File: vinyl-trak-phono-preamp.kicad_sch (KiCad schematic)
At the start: 79 parts, among them J1 Conn_01x03_Pin, J2 Screw_Terminal_01x03, J3 Screw_Terminal_01x02, J4 Screw_Terminal_01x02, Q1 2N3906, Q10 2N3906, Q11 JFE2140D, Q12 2N5089, Q13 2N3904, Q14 2N3904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

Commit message: Revision 0.1
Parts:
- removed C1: 0.015u, symbol Device:C
- removed C2: 100p, Capacitor_SMD:C_0805_2012Metric_Pad1.18x1.45mm_HandSolder, symbol Device:C
- removed C3: 0.005u, symbol Device:C
- removed C4: 0.015u, Capacitor_SMD:C_0805_2012Metric_Pad1.18x1.45mm_HandSolder, symbol Device:C
- removed C6: 1u, Capacitor_SMD:C_0805_2012Metric_Pad1.18x1.45mm_HandSolder, symbol Device:C
- removed C7, C8: 10n, Capacitor_SMD:C_0805_2012Metric_Pad1.18x1.45mm_HandSolder, symbol Device:C
- removed C9: 0.020u, Capacitor_SMD:C_0805_2012Metric_Pad1.18x1.45mm_HandSolder, symbol Device:C
- removed D1, D2: D, Diode_SMD:D_0805_2012Metric_Pad1.15x1.40mm_HandSolder, symbol Device:D
- removed J1: Conn_01x03_Pin, Connector_PinHeader_1.27mm:PinHeader_1x03_P1.27mm_Vertical, symbol Connector:Conn_01x03_Pin
- removed J2: Screw_Terminal_01x03, TerminalBlock_4Ucon:TerminalBlock_4Ucon_1x03_P3.50mm_Horizontal, symbol Connector:Screw_Terminal_01x03
- removed J3: Screw_Terminal_01x02, TerminalBlock_4Ucon:TerminalBlock_4Ucon_1x02_P3.50mm_Horizontal, symbol Connector:Screw_Terminal_01x02
- removed Q1, Q10, Q3, Q4, Q8: 2N3906, Library:SOT-23_Handsoldering-adjusted-pinout, symbol Simulation_SPICE:PNP
- removed Q11: JFE2140D, Package_SO:SOIC-8_3.9x4.9mm_P1.27mm, symbol Transistor_FET:JFE2140D
- removed Q12, Q15, Q18, Q19, Q21: 2N5089, Library:SOT-23_Handsoldering-adjusted-pinout, symbol Simulation_SPICE:NPN
- removed Q13, Q14, Q2, Q5, Q6, Q7, Q9: 2N3904, Library:SOT-23_Handsoldering-adjusted-pinout, symbol Simulation_SPICE:NPN
- removed Q16, Q17, Q20: 2N5087, Library:SOT-23_Handsoldering-adjusted-pinout, symbol Simulation_SPICE:PNP
- removed R1, R3: 100k, Resistor_SMD:R_0805_2012Metric_Pad1.20x1.40mm_HandSolder, symbol Device:R
- removed R10, R11: 600, Resistor_SMD:R_0805_2012Metric_Pad1.20x1.40mm_HandSolder, symbol Device:R
- removed R12, R13, R17, R8, R9: 220, Resistor_SMD:R_0805_2012Metric_Pad1.20x1.40mm_HandSolder, symbol Device:R
- removed R14, R19, R23, R24: 1k47, Resistor_SMD:R_0805_2012Metric_Pad1.20x1.40mm_HandSolder, symbol Device:R
- removed R15, R20: 100, Resistor_SMD:R_0805_2012Metric_Pad1.20x1.40mm_HandSolder, symbol Device:R
- removed R16: 71k5, Resistor_SMD:R_0805_2012Metric_Pad1.20x1.40mm_HandSolder, symbol Device:R
- removed R18: 160, Resistor_SMD:R_0805_2012Metric_Pad1.20x1.40mm_HandSolder, symbol Device:R
- removed R2: 18k, Resistor_SMD:R_0805_2012Metric_Pad1.20x1.40mm_HandSolder, symbol Device:R
- removed R21, R34: 56k2, Resistor_SMD:R_0805_2012Metric_Pad1.20x1.40mm_HandSolder, symbol Device:R
- removed R22: 2.2Meg, Resistor_SMD:R_0805_2012Metric_Pad1.20x1.40mm_HandSolder, symbol Device:R
- removed R25: 15k0, Resistor_SMD:R_0805_2012Metric_Pad1.20x1.40mm_HandSolder, symbol Device:R
- removed R26: 162k, Resistor_SMD:R_0805_2012Metric_Pad1.20x1.40mm_HandSolder, symbol Device:R
- removed R27, R31: 1k78, Resistor_SMD:R_0805_2012Metric_Pad1.20x1.40mm_HandSolder, symbol Device:R
- removed R28: 1Meg, Resistor_SMD:R_0805_2012Metric_Pad1.20x1.40mm_HandSolder, symbol Device:R
- removed R29: 3k83, Resistor_SMD:R_0805_2012Metric_Pad1.20x1.40mm_HandSolder, symbol Device:R
- removed R30: 47.5k, Resistor_SMD:R_0805_2012Metric_Pad1.20x1.40mm_HandSolder, symbol Device:R
- removed R33: 20k, Resistor_SMD:R_0805_2012Metric_Pad1.20x1.40mm_HandSolder, symbol Device:R
- removed R35: 33.2k, Resistor_SMD:R_0805_2012Metric_Pad1.20x1.40mm_HandSolder, symbol Device:R
- removed R36: 115k, Resistor_SMD:R_0805_2012Metric_Pad1.20x1.40mm_HandSolder, symbol Device:R
- removed R37, R38: 1, Resistor_SMD:R_0805_2012Metric_Pad1.20x1.40mm_HandSolder, symbol Device:R
- removed R6: 1k37, Resistor_SMD:R_0805_2012Metric_Pad1.20x1.40mm_HandSolder, symbol Device:R
- removed R7: 205k, Resistor_SMD:R_0805_2012Metric_Pad1.20x1.40mm_HandSolder, symbol Device:R
- removed U1: OPA2134, Package_SO:SOIC-8_3.9x4.9mm_P1.27mm, symbol Amplifier_Operational:OPA2134
- added C18: 100p, symbol Device:C
- added J11, J12, J13, J7, J8: Screw_Terminal_01x02, Library:TerminalBlock_4Ucon_1x02_P5mm_Horizontal, symbol Connector:Screw_Terminal_01x02
- added L3, L4: 350m, symbol Device:L
- added R73, R74: 650, symbol Device:R
- added V2: 0, symbol Simulation_SPICE:VDC
- J4: footprint TerminalBlock_4Ucon:TerminalBlock_4Ucon_1x02_P3.50mm_Horizontal -> Library:TerminalBlock_4Ucon_1x02_P5mm_Horizontal
- V1: value 0 -> (none)
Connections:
- net +15V: now also J11.2 (Pin_2)
- net -15: now also J11.1 (Pin_1)
- net 0: now also J7.1 (Pin_1), J8.1 (Pin_1), J8.2 (Pin_2)
- net cartridge+ renamed l-in+
- net l-in+: now also J13.2 (Pin_2)
- net cartridge- renamed l-in-
- net l-in-: now also J13.1 (Pin_1)
- net out renamed l-out
- new net: R74.1, V2.2
- new net: L4.1, R74.2
- new net: R73.1, V2.1
- new net: L3.1, R73.2
- new net r-in+: C18.1, J12.2 (Pin_2), L3.2
- new net r-in-: C18.2, J12.1 (Pin_1), L4.2
- new net r-out: J7.2 (Pin_2)
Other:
- added sheet phono-in-left (phono-in.kicad_sch)
- added sheet phono-in-right (phono-in.kicad_sch)
- note removed: "Cartridge loading"
- note removed: "Cascode filter Option 1 (conventional)"
- note removed: "Cascode filter Option 2 (overdamped 75us)"
- note removed: "Diamond Buffer"
- note removed: "Differential amplifier"
- note removed: "VAS"
- moved on the sheet: C5, J4, V4, V5

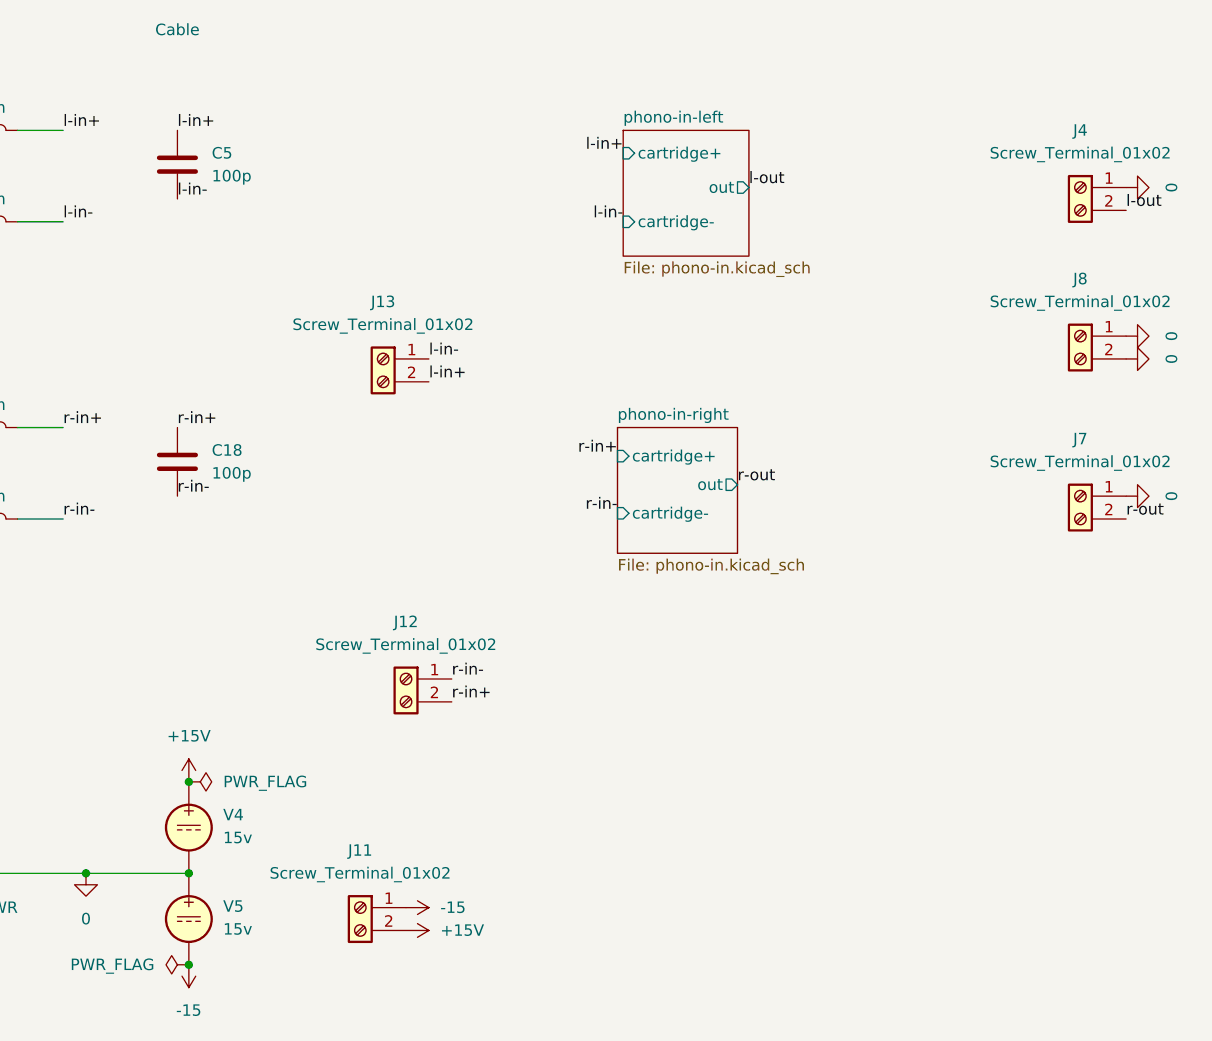
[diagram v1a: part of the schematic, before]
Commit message: Revision 0.2
- TH components mounted to PCB back to preserve front space
- 15+ and 15- lines are kept closer together to reduce noise (even though di/dt is relatively low)
- Signal path bends around PCB area; DC servo feedback path is much shorter
- Signal path kept on first layer without jumpers

- Power distribution is messy
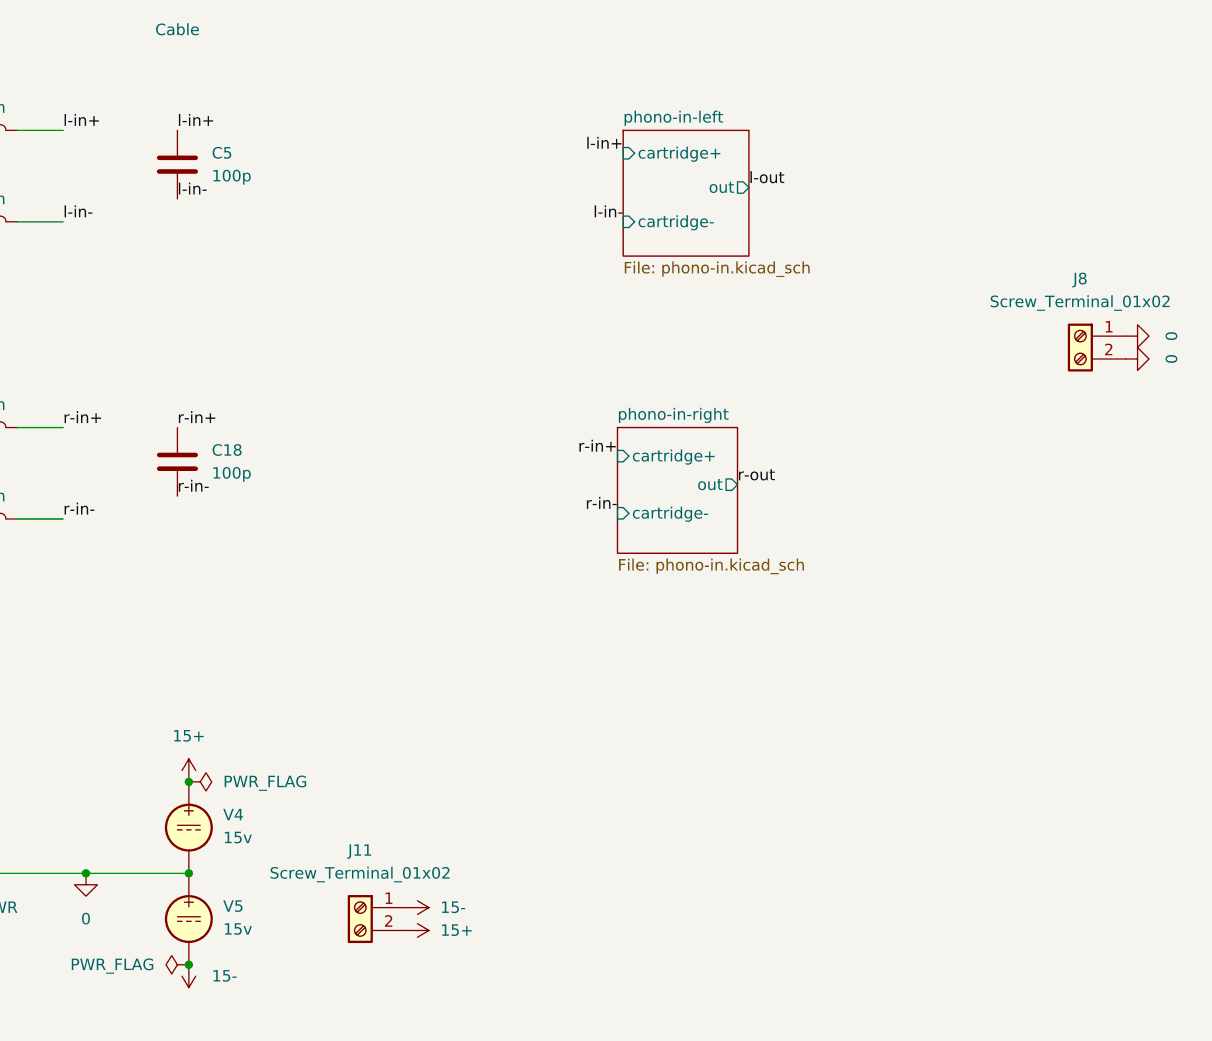
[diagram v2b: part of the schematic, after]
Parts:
- removed J12, J13, J4, J7: Screw_Terminal_01x02, Library:TerminalBlock_4Ucon_1x02_P5mm_Horizontal, symbol Connector:Screw_Terminal_01x02
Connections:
- net +15V renamed 15+
- net -15 renamed 15-
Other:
- title: (none) -> VinylTrak MM Phono Input Stage
